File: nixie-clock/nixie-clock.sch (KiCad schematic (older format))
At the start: 26 parts

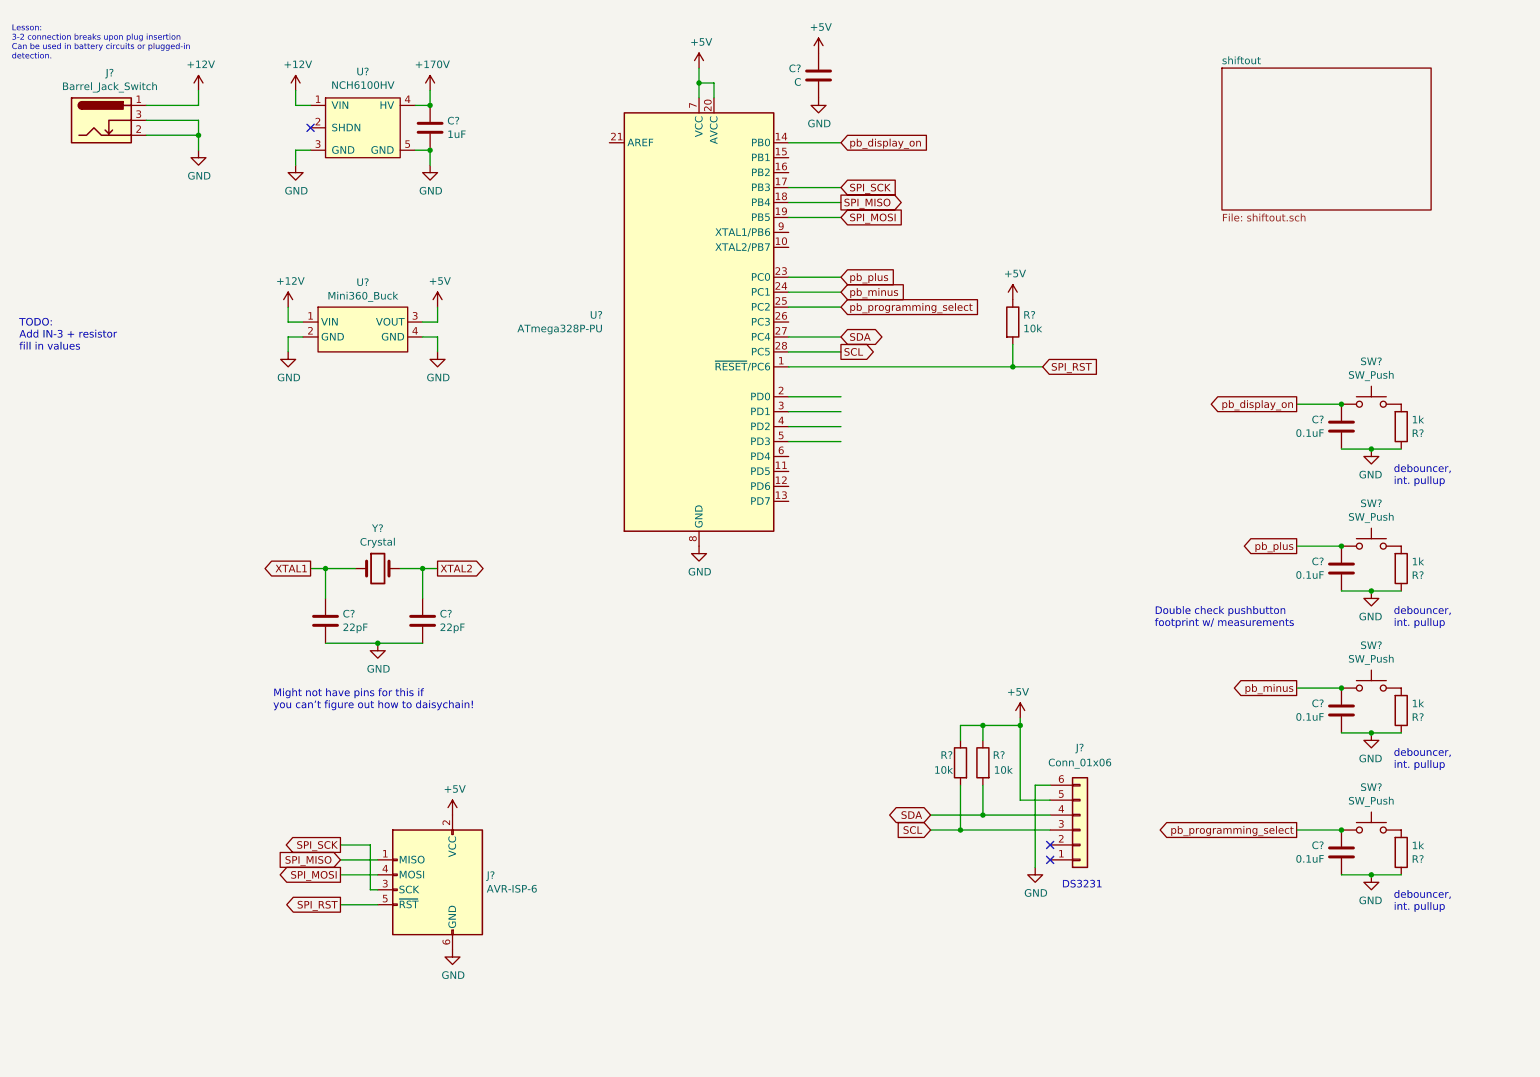
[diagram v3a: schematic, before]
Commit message: Finished schematic for nixie clock main board. Added IN-3 footprint.
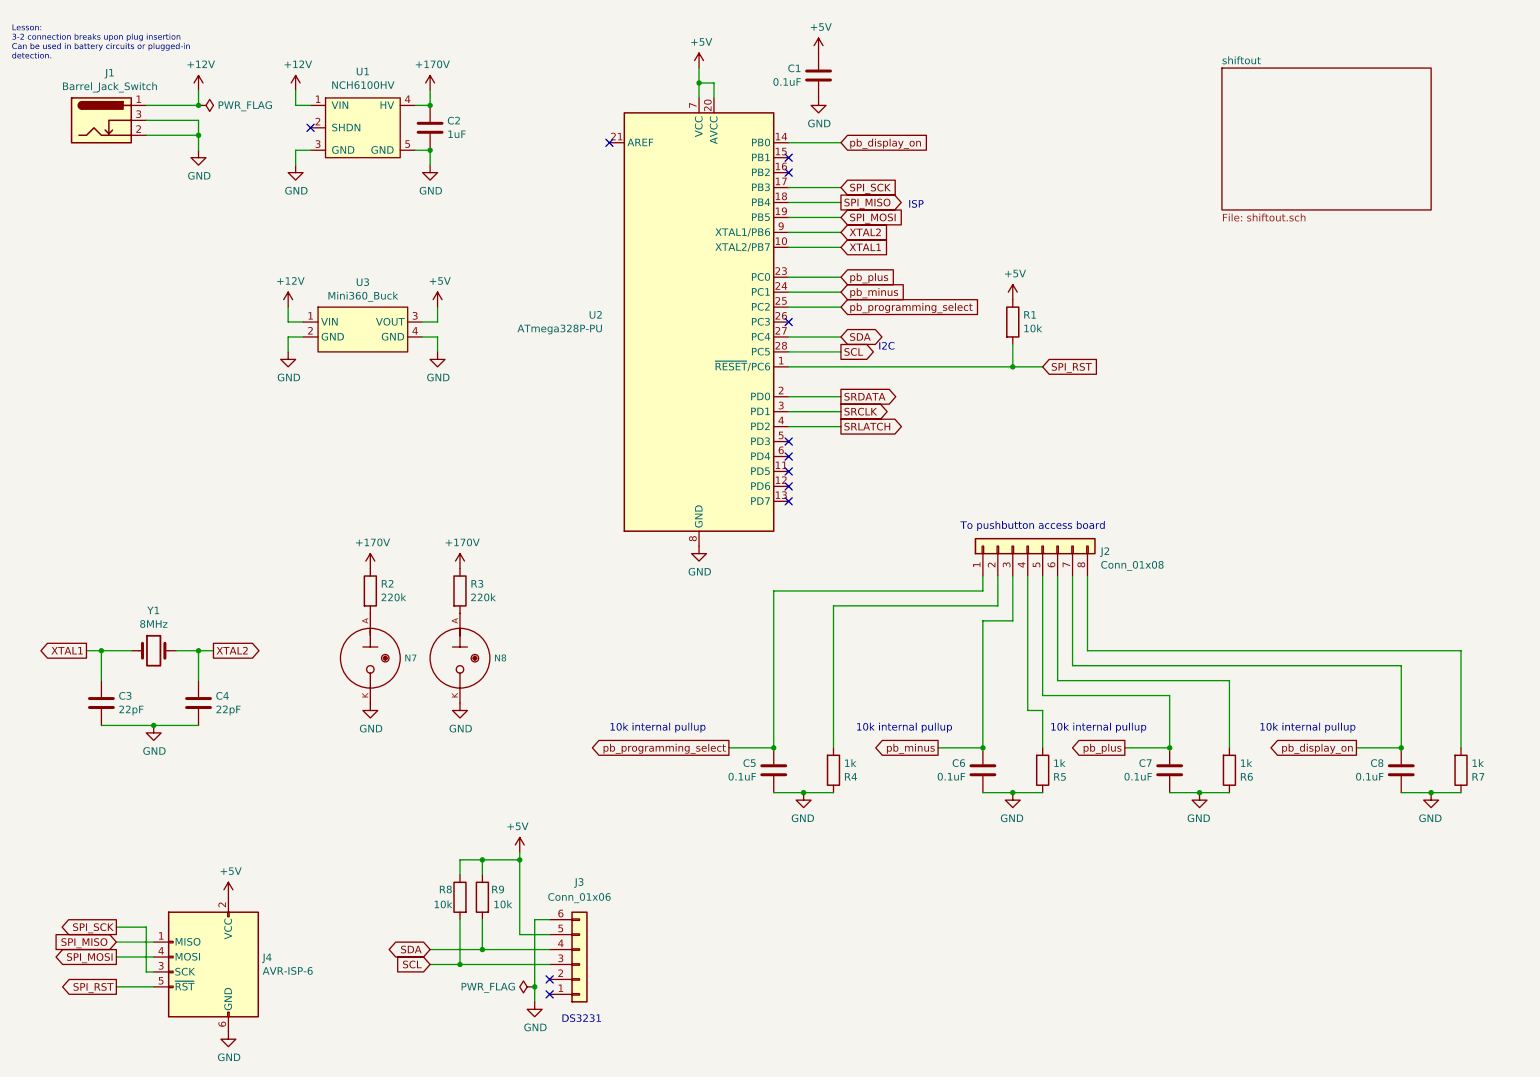
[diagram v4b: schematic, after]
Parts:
- removed SW? (x4): SW_Push, Button_Switch_THT:SW_PUSH_6mm, symbol Switch:SW_Push
- added J2: Conn_01x08, Connector_PinHeader_2.54mm:PinHeader_2x04_P2.54mm_Vertical, symbol Connector_Generic:Conn_01x08
- added N7, N8: IN-3, footprints-nad:IN-3_Bare, symbol nixies-us:IN-3
- added R2, R3: 220k, Resistor_THT:R_Axial_DIN0207_L6.3mm_D2.5mm_P10.16mm_Horizontal, symbol Device:R
- C1: renamed from C?; value C -> 0.1uF; footprint (none) -> Capacitor_THT:C_Disc_D5.0mm_W2.5mm_P5.00mm
- C3, C4: renamed from C?; footprint (none) -> Capacitor_THT:C_Disc_D3.0mm_W2.0mm_P2.50mm
- C5, C6, C7, C8: renamed from C?; footprint (none) -> Capacitor_THT:C_Disc_D5.0mm_W2.5mm_P5.00mm
- R1, R4, R5, R6, R7, R8, R9: renamed from R?; footprint (none) -> Resistor_THT:R_Axial_DIN0207_L6.3mm_D2.5mm_P10.16mm_Horizontal
- U3: renamed from U?; footprint (none) -> footprints-nad:Mini360_PinSockets
- Y1: renamed from Y?; value Crystal -> 8MHz; footprint (none) -> Crystal:Crystal_HC49-4H_Vertical
- gave numbers to parts that had none: 6
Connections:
- net labels added: SRCLK, SRDATA, SRLATCH
- wire segments 83 -> 109
- no-connect marks 3 -> 12
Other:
- note added: "10k internal pullup"
- note added: "I2C"
- note added: "ISP"
- note added: "To pushbutton access board"
- note removed: "Double check pushbutton\nfootprint w/ measurements"
- note removed: "Might not have pins for this if \nyou can’t figure out how to daisychain!"
- note removed: "TODO:\nAdd IN-3 + resistor\nfill in values\n"
- note removed: "debouncer,\nint. pullup"
- moved on the sheet: C3, C4, C5, C6, C7, C8, J3, J4, R4, R5, R6, R7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

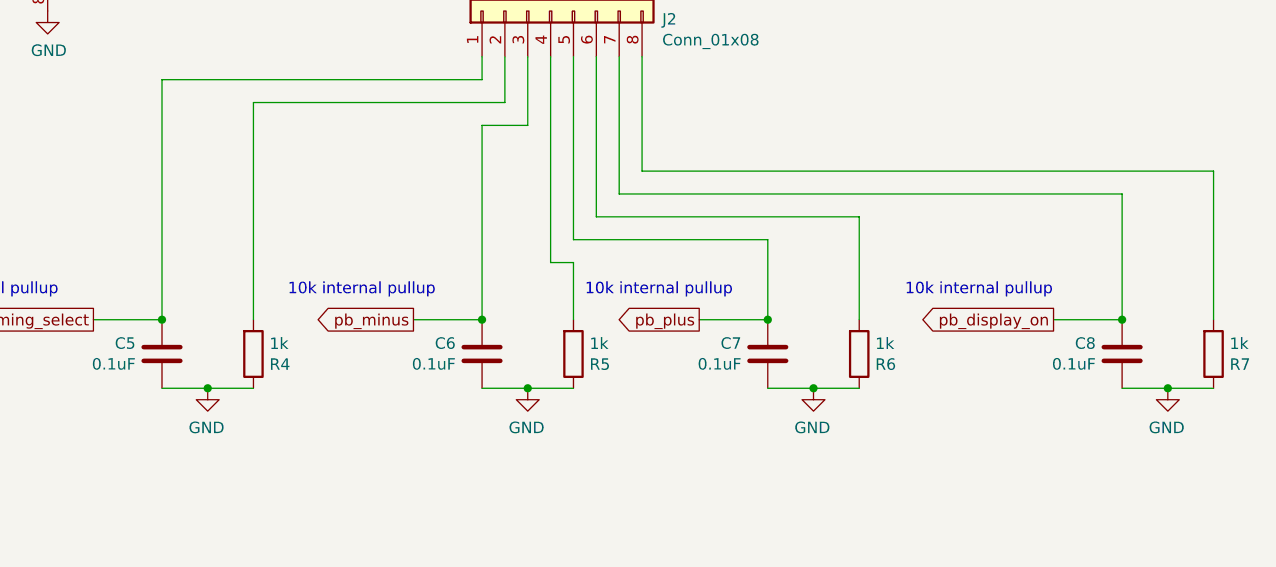
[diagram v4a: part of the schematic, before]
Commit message: Readded pushbuttons to mainboard as an option. Beginning K155ID1-nixie exchange zone.
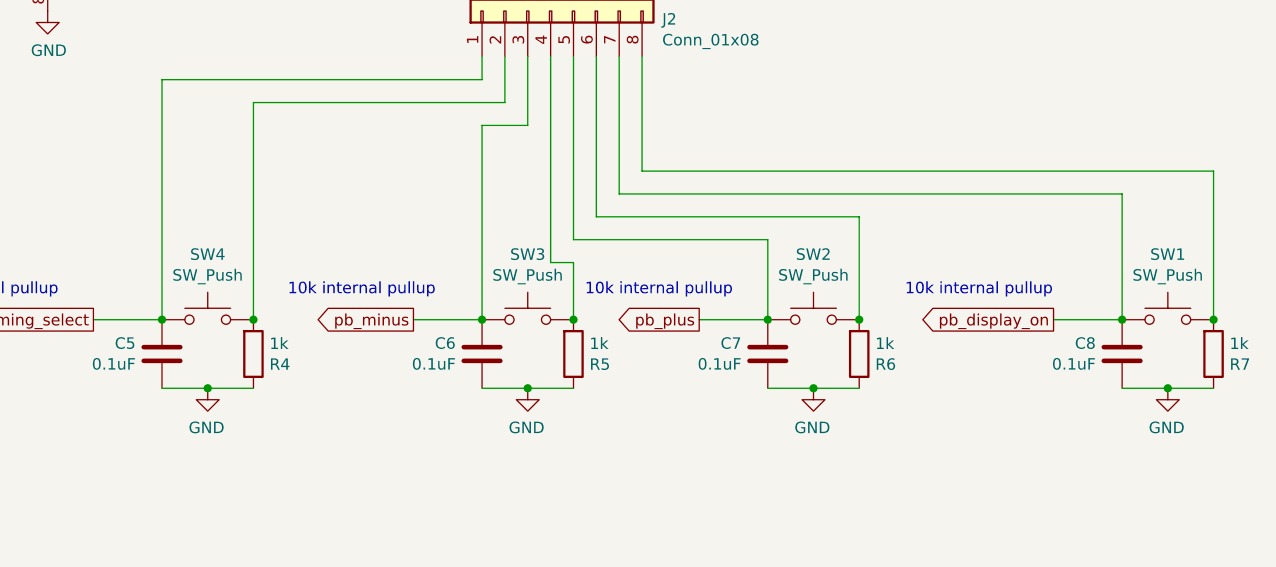
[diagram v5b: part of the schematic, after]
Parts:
- added SW1, SW2, SW3, SW4: SW_Push, Button_Switch_THT:SW_PUSH_6mm, symbol Switch:SW_Push
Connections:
- net pb_display_on: now also SW1.1
- net pb_minus: now also SW3.1
- net pb_plus: now also SW2.1
- net pb_programming_select: now also SW4.1
- net at J2.4 (Pin_4), R5.2: now also SW3.2
- net at J2.2 (Pin_2), R4.2: now also SW4.2
- net at J2.8 (Pin_8), R7.2: now also SW1.2
- net at J2.6 (Pin_6), R6.2: now also SW2.2
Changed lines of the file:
@@
 Text Notes 6600 1900 0    50   ~ 0
 ISP
+$Comp
+L Switch:SW_Push SW4
+U 1 1 5EA51322
+P 5900 5500
+F 0 "SW4" H 5900 5785 50  0000 C CNN
+F 1 "SW_Push" H 5900 5694 50  0000 C CNN
+F 2 "Button_Switch_THT:SW_PUSH_6mm" H 5900 5700 50  0001 C CNN
+F 3 "~" H 5900 5700 50  0001 C CNN
+	1    5900 5500
+	1    0    0    -1
+$EndComp
+Connection ~ 6100 5500
+$Comp
+L Switch:SW_Push SW3
+U 1 1 5EA51ACC
+P 7300 5500
+F 0 "SW3" H 7300 5785 50  0000 C CNN
+F 1 "SW_Push" H 7300 5694 50  0000 C CNN
+F 2 "Button_Switch_THT:SW_PUSH_6mm" H 7300 5700 50  0001 C CNN
+F 3 "~" H 7300 5700 50  0001 C CNN
+	1    7300 5500
+	1    0    0    -1
+$EndComp
+Connection ~ 7500 5500
+$Comp
+L Switch:SW_Push SW2
+U 1 1 5EA520BA
+P 8550 5500
+F 0 "SW2" H 8550 5785 50  0000 C CNN
+F 1 "SW_Push" H 8550 5694 50  0000 C CNN
+F 2 "Button_Switch_THT:SW_PUSH_6mm" H 8550 5700 50  0001 C CNN
+F 3 "~" H 8550 5700 50  0001 C CNN
+	1    8550 5500
+	1    0    0    -1
+$EndComp
+Connection ~ 8750 5500
+$Comp
+L Switch:SW_Push SW1
+U 1 1 5EA526A8
+P 10100 5500
+F 0 "SW1" H 10100 5785 50  0000 C CNN
+F 1 "SW_Push" H 10100 5694 50  0000 C CNN
+F 2 "Button_Switch_THT:SW_PUSH_6mm" H 10100 5700 50  0001 C CNN
+F 3 "~" H 10100 5700 50  0001 C CNN
+	1    10100 5500
+	1    0    0    -1
+$EndComp
+Connection ~ 10300 5500
 $EndSCHEMATC

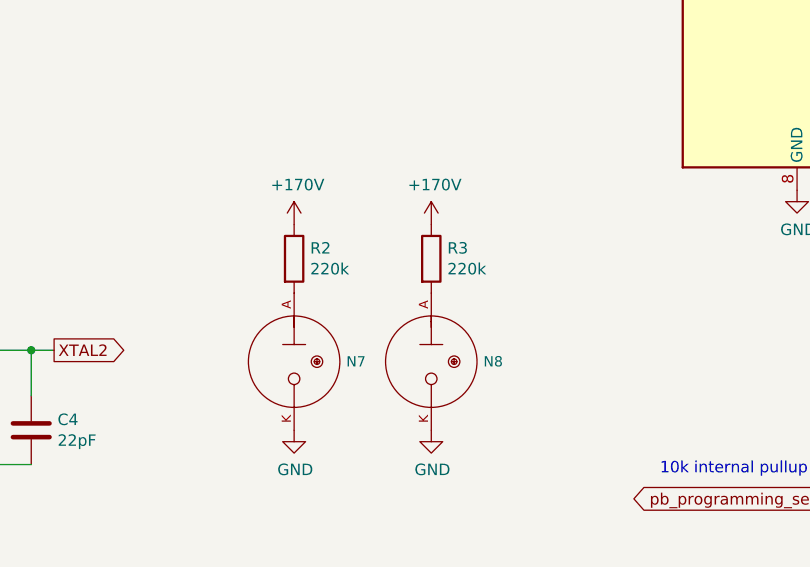
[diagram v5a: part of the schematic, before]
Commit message: Fixed anode net names. Finished routing anode connections.
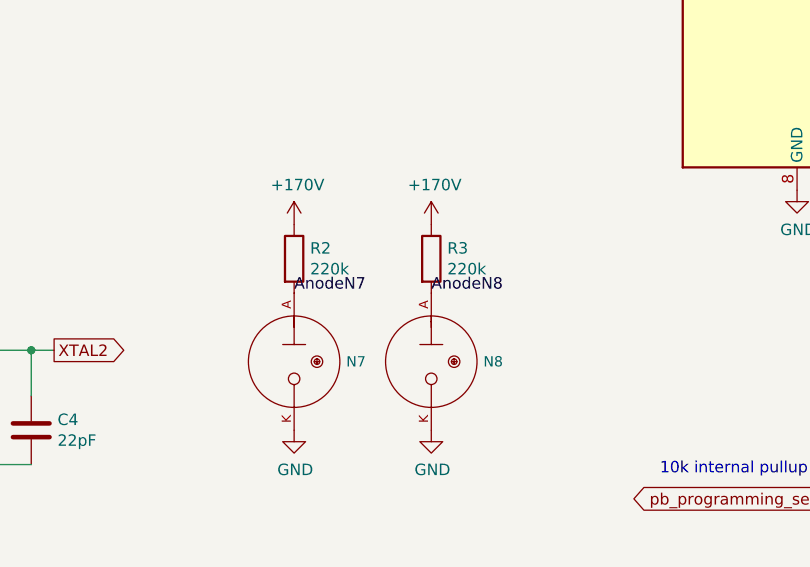
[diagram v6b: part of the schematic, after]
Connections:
- net AnodeN7: now reaches N7.A, R2.2
- net AnodeN8: now reaches N8.A, R3.2
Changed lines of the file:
@@
 $EndComp
 Connection ~ 10300 5500
+Text Label 3000 4600 0    50   ~ 0
+AnodeN7
+Text Label 3600 4600 0    50   ~ 0
+AnodeN8
 $EndSCHEMATC

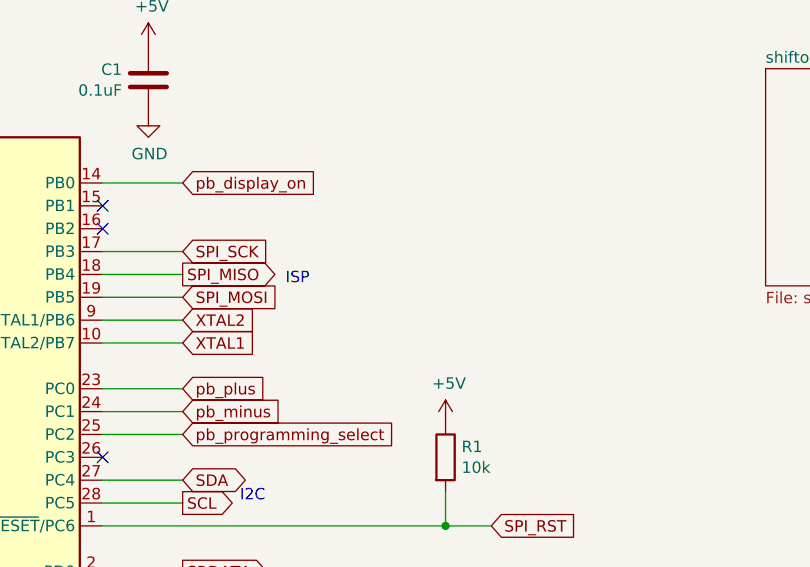
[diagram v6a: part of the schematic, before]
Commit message: ISP ports CLK & MOSI were wrong. Added blurb to note that its wrong. Didnt change it to reflect what the board actually has since I'm not going to make another rev.
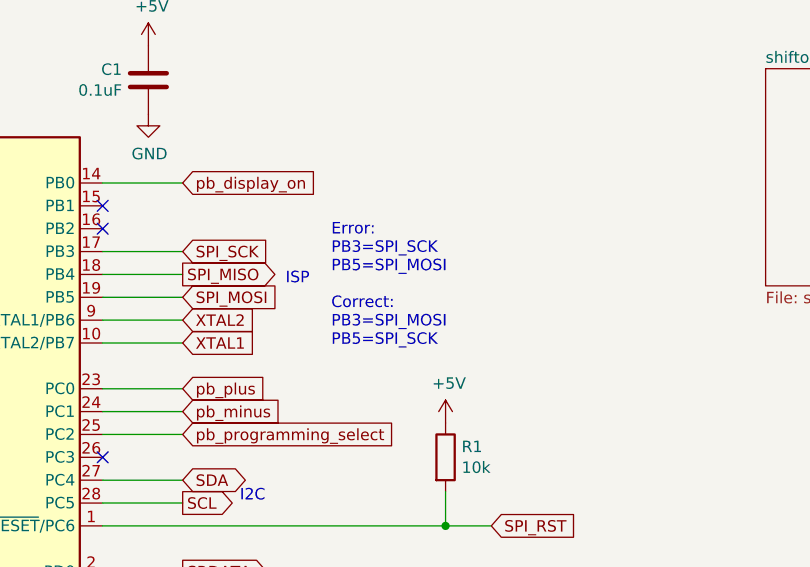
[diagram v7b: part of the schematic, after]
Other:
- note added: "Error: \nPB3=SPI_SCK\nPB5=SPI_MOSI\n\nCorrect:\nPB3=SPI_MOSI\nPB5=SPI_SCK\n\n"
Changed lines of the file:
@@
 Text GLabel 1300 7100 0    50   Output ~ 0
 SPI_RST
-Text GLabel 6150 1950 2    50   Input ~ 0
-SPI_MOSI
 Text GLabel 6150 1850 2    50   Output ~ 0
 SPI_MISO
-Text GLabel 6150 1750 2    50   Input ~ 0
-SPI_SCK
 Wire Wire Line
 	5800 1750 6150 1750
@@
 Text Label 3600 4600 0    50   ~ 0
 AnodeN8
+Text Notes 6800 2250 0    50   ~ 0
+Error: \nPB3=SPI_SCK\nPB5=SPI_MOSI\n\nCorrect:\nPB3=SPI_MOSI\nPB5=SPI_SCK\n\n
+Text GLabel 6150 1750 2    50   Input ~ 0
+SPI_SCK
+Text GLabel 6150 1950 2    50   Input ~ 0
+SPI_MOSI
 $EndSCHEMATC
